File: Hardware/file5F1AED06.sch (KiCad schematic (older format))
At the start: 17 parts, among them U2 RFPA3800

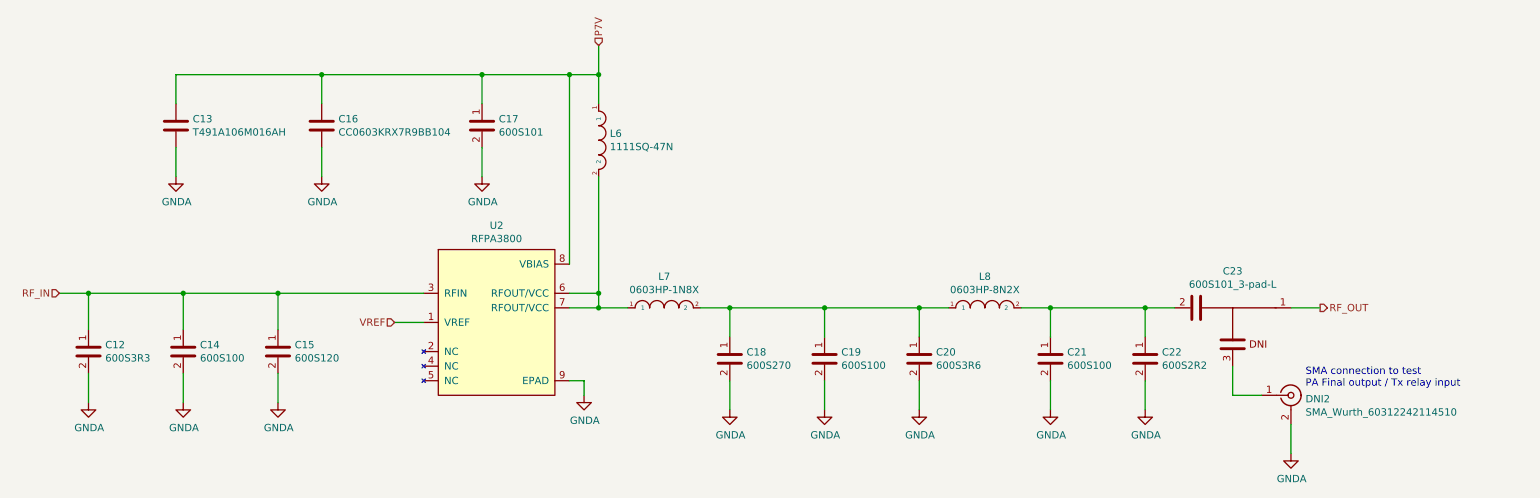
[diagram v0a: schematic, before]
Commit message: Added discrete Chebyshev input filter to schematic based on Qucs simulationd. Artwork not done. It has occurred to me that I need to do some major cleanup of the test points on this PCBA.
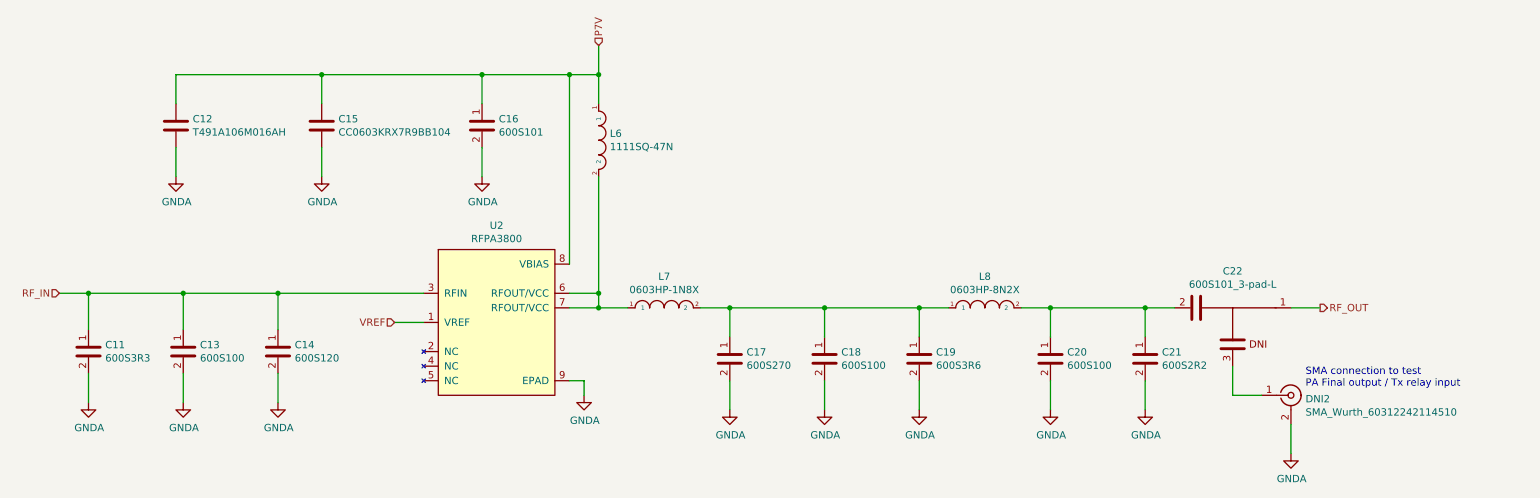
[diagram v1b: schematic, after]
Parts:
- renumbered C12 to C11, C13 to C12, C14 to C13, C15 to C14, C16 to C15, C17 to C16, C18 to C17, C19 to C18, C20 to C19, C21 to C20, C22 to C21, C23 to C22
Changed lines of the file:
@@
 $Descr A4 11693 8268
 encoding utf-8
-Sheet 7 12
+Sheet 7 16
 Title ""
 Date ""
@@
 P 4900 4600
 AR Path="/5F04F5B6/5F1D8FAC" Ref="#PWR?"  Part="1"
-AR Path="/5F04F5B6/5F1AED07/5F1D8FAC" Ref="#PWR026"  Part="1"
-F 0 "#PWR026" H 4900 4350 50  0001 C CNN
+AR Path="/5F04F5B6/5F1AED07/5F1D8FAC" Ref="#PWR023"  Part="1"
+F 0 "#PWR023" H 4900 4350 50  0001 C CNN
 F 1 "GNDA" H 4905 4427 50  0000 C CNN
 F 2 "" H 4900 4600 50  0001 C CNN
@@
 AR Path="/5F19ABE9/5F1D8FD9" Ref="#PWR?"  Part="1"
 AR Path="/5F04F5B6/5F1D8FD9" Ref="#PWR?"  Part="1"
-AR Path="/5F04F5B6/5F1AED07/5F1D8FD9" Ref="#PWR030"  Part="1"
-F 0 "#PWR030" H 8100 4450 50  0001 C CNN
+AR Path="/5F04F5B6/5F1AED07/5F1D8FD9" Ref="#PWR027"  Part="1"
+F 0 "#PWR027" H 8100 4450 50  0001 C CNN
 F 1 "GNDA" H 8105 4527 50  0000 C CNN
 F 2 "" H 8100 4700 50  0001 C CNN
@@
 AR Path="/5F19ABE9/5F1D8FEC" Ref="C?"  Part="1"
 AR Path="/5F04F5B6/5F1D8FEC" Ref="C?"  Part="1"
-AR Path="/5F04F5B6/5F1AED07/5F1D8FEC" Ref="C17"  Part="1"
-F 0 "C17" H 4315 2796 50  0000 L CNN
+AR Path="/5F04F5B6/5F1AED07/5F1D8FEC" Ref="C16"  Part="1"
+F 0 "C16" H 4315 2796 50  0000 L CNN
 F 1 "600S101" H 4315 2705 50  0000 L CNN
 F 2 "Resistor_SMD:R_0603_1608Metric" H 4250 2850 50  0001 C CNN
@@
 AR Path="/5F19ABE9/5F1D8FF2" Ref="#PWR?"  Part="1"
 AR Path="/5F04F5B6/5F1D8FF2" Ref="#PWR?"  Part="1"
-AR Path="/5F04F5B6/5F1AED07/5F1D8FF2" Ref="#PWR024"  Part="1"
-F 0 "#PWR024" H 3100 2850 50  0001 C CNN
+AR Path="/5F04F5B6/5F1AED07/5F1D8FF2" Ref="#PWR021"  Part="1"
+F 0 "#PWR021" H 3100 2850 50  0001 C CNN
 F 1 "GNDA" H 3105 2927 50  0000 C CNN
 F 2 "" H 3100 3100 50  0001 C CNN
@@
 AR Path="/5F19ABE9/5F1D8FF9" Ref="#PWR?"  Part="1"
 AR Path="/5F04F5B6/5F1D8FF9" Ref="#PWR?"  Part="1"
-AR Path="/5F04F5B6/5F1AED07/5F1D8FF9" Ref="#PWR025"  Part="1"
-F 0 "#PWR025" H 4200 2850 50  0001 C CNN
+AR Path="/5F04F5B6/5F1AED07/5F1D8FF9" Ref="#PWR022"  Part="1"
+F 0 "#PWR022" H 4200 2850 50  0001 C CNN
 F 1 "GNDA" H 4205 2927 50  0000 C CNN
 F 2 "" H 4200 3100 50  0001 C CNN
@@
 P 3100 2750
 AR Path="/5F04F5B6/5F1D9008" Ref="C?"  Part="1"
-AR Path="/5F04F5B6/5F1AED07/5F1D9008" Ref="C16"  Part="1"
-F 0 "C16" H 3215 2796 50  0000 L CNN
+AR Path="/5F04F5B6/5F1AED07/5F1D9008" Ref="C15"  Part="1"
+F 0 "C15" H 3215 2796 50  0000 L CNN
 F 1 "CC0603KRX7R9BB104" H 3215 2705 50  0000 L CNN
 F 2 "Capacitor_SMD:C_0603_1608Metric" H 3138 2600 50  0001 C CNN
@@
 P 2150 4300
 AR Path="/5F04F5B6/5F1D9016" Ref="C?"  Part="1"
-AR Path="/5F04F5B6/5F1AED07/5F1D9016" Ref="C14"  Part="1"
-F 0 "C14" H 2265 4346 50  0000 L CNN
+AR Path="/5F04F5B6/5F1AED07/5F1D9016" Ref="C13"  Part="1"
+F 0 "C13" H 2265 4346 50  0000 L CNN
 F 1 "600S100" H 2265 4255 50  0000 L CNN
 F 2 "Capacitor_SMD:C_0603_1608Metric" H 2200 4400 50  0001 C CNN
@@
 P 2800 4300
 AR Path="/5F04F5B6/5F1D901C" Ref="C?"  Part="1"
-AR Path="/5F04F5B6/5F1AED07/5F1D901C" Ref="C15"  Part="1"
-F 0 "C15" H 2915 4346 50  0000 L CNN
+AR Path="/5F04F5B6/5F1AED07/5F1D901C" Ref="C14"  Part="1"
+F 0 "C14" H 2915 4346 50  0000 L CNN
 F 1 "600S120" H 2915 4255 50  0000 L CNN
 F 2 "Capacitor_SMD:C_0603_1608Metric" H 2850 4400 50  0001 C CNN
@@
 P 1500 4300
 AR Path="/5F04F5B6/5F1D9022" Ref="C?"  Part="1"
-AR Path="/5F04F5B6/5F1AED07/5F1D9022" Ref="C12"  Part="1"
-F 0 "C12" H 1615 4346 50  0000 L CNN
+AR Path="/5F04F5B6/5F1AED07/5F1D9022" Ref="C11"  Part="1"
+F 0 "C11" H 1615 4346 50  0000 L CNN
 F 1 "600S3R3" H 1615 4255 50  0000 L CNN
 F 2 "Capacitor_SMD:C_0603_1608Metric" H 1550 4400 50  0001 C CNN
@@
 RF_IN
 $Comp
-L power:GNDA #PWR020
+L power:GNDA #PWR017
 U 1 1 5F1E2B17
 P 1500 4650
-F 0 "#PWR020" H 1500 4400 50  0001 C CNN
+F 0 "#PWR017" H 1500 4400 50  0001 C CNN
 F 1 "GNDA" H 1505 4477 50  0000 C CNN
 F 2 "" H 1500 4650 50  0001 C CNN
@@
 $EndComp
 $Comp
-L power:GNDA #PWR022
+L power:GNDA #PWR019
 U 1 1 5F1E2D76
 P 2150 4650
-F 0 "#PWR022" H 2150 4400 50  0001 C CNN
+F 0 "#PWR019" H 2150 4400 50  0001 C CNN
 F 1 "GNDA" H 2155 4477 50  0000 C CNN
 F 2 "" H 2150 4650 50  0001 C CNN
@@
 $EndComp
 $Comp
-L power:GNDA #PWR023
+L power:GNDA #PWR020
 U 1 1 5F1E3182
 P 2800 4650
-F 0 "#PWR023" H 2800 4400 50  0001 C CNN
+F 0 "#PWR020" H 2800 4400 50  0001 C CNN
 F 1 "GNDA" H 2805 4477 50  0000 C CNN
 F 2 "" H 2800 4650 50  0001 C CNN
@@
 $EndComp
 $Comp
-L ATC:600S270 C18
+L ATC:600S270 C17
 U 1 1 5F1EB80A
 P 5900 4350
-F 0 "C18" H 6015 4396 50  0000 L CNN
+F 0 "C17" H 6015 4396 50  0000 L CNN
 F 1 "600S270" H 6015 4305 50  0000 L CNN
 F 2 "Capacitor_SMD:C_0603_1608Metric" H 5950 4450 50  0001 C CNN
@@
 $EndComp
 $Comp
-L ATC:600S100 C19
+L ATC:600S100 C18
 U 1 1 5F1EBBE5
 P 6550 4350
-F 0 "C19" H 6665 4396 50  0000 L CNN
+F 0 "C18" H 6665 4396 50  0000 L CNN
 F 1 "600S100" H 6665 4305 50  0000 L CNN
 F 2 "Capacitor_SMD:C_0603_1608Metric" H 6600 4450 50  0001 C CNN
@@
 $EndComp
 $Comp
-L ATC:600S3R6 C20
+L ATC:600S3R6 C19
 U 1 1 5F1EBFC8
 P 7200 4350
-F 0 "C20" H 7315 4396 50  0000 L CNN
+F 0 "C19" H 7315 4396 50  0000 L CNN
 F 1 "600S3R6" H 7315 4305 50  0000 L CNN
 F 2 "Capacitor_SMD:C_0603_1608Metric" H 7250 4450 50  0001 C CNN
@@
 $EndComp
 $Comp
-L ATC:600S100 C21
+L ATC:600S100 C20
 U 1 1 5F1EC703
 P 8100 4350
-F 0 "C21" H 8215 4396 50  0000 L CNN
+F 0 "C20" H 8215 4396 50  0000 L CNN
 F 1 "600S100" H 8215 4305 50  0000 L CNN
 F 2 "Capacitor_SMD:C_0603_1608Metric" H 8150 4450 50  0001 C CNN
@@
 $EndComp
 $Comp
-L ATC:600S2R2 C22
+L ATC:600S2R2 C21
 U 1 1 5F1ECAB0
 P 8750 4350
-F 0 "C22" H 8865 4396 50  0000 L CNN
+F 0 "C21" H 8865 4396 50  0000 L CNN
 F 1 "600S2R2" H 8865 4305 50  0000 L CNN
 F 2 "Capacitor_SMD:C_0603_1608Metric" H 8800 4450 50  0001 C CNN
@@
 AR Path="/5F19ABE9/5F1F33B9" Ref="#PWR?"  Part="1"
 AR Path="/5F04F5B6/5F1F33B9" Ref="#PWR?"  Part="1"
-AR Path="/5F04F5B6/5F1AED07/5F1F33B9" Ref="#PWR029"  Part="1"
-F 0 "#PWR029" H 7200 4450 50  0001 C CNN
+AR Path="/5F04F5B6/5F1AED07/5F1F33B9" Ref="#PWR026"  Part="1"
+F 0 "#PWR026" H 7200 4450 50  0001 C CNN
 F 1 "GNDA" H 7205 4527 50  0000 C CNN
 F 2 "" H 7200 4700 50  0001 C CNN
@@
 AR Path="/5F19ABE9/5F1F3A81" Ref="#PWR?"  Part="1"
 AR Path="/5F04F5B6/5F1F3A81" Ref="#PWR?"  Part="1"
-AR Path="/5F04F5B6/5F1AED07/5F1F3A81" Ref="#PWR028"  Part="1"
-F 0 "#PWR028" H 6550 4450 50  0001 C CNN
+AR Path="/5F04F5B6/5F1AED07/5F1F3A81" Ref="#PWR025"  Part="1"
+F 0 "#PWR025" H 6550 4450 50  0001 C CNN
 F 1 "GNDA" H 6555 4527 50  0000 C CNN
 F 2 "" H 6550 4700 50  0001 C CNN
@@
 AR Path="/5F19ABE9/5F1F436D" Ref="#PWR?"  Part="1"
 AR Path="/5F04F5B6/5F1F436D" Ref="#PWR?"  Part="1"
-AR Path="/5F04F5B6/5F1AED07/5F1F436D" Ref="#PWR027"  Part="1"
-F 0 "#PWR027" H 5900 4450 50  0001 C CNN
+AR Path="/5F04F5B6/5F1AED07/5F1F436D" Ref="#PWR024"  Part="1"
+F 0 "#PWR024" H 5900 4450 50  0001 C CNN
 F 1 "GNDA" H 5905 4527 50  0000 C CNN
 F 2 "" H 5900 4700 50  0001 C CNN
@@
 AR Path="/5F19ABE9/5F1F4C55" Ref="#PWR?"  Part="1"
 AR Path="/5F04F5B6/5F1F4C55" Ref="#PWR?"  Part="1"
-AR Path="/5F04F5B6/5F1AED07/5F1F4C55" Ref="#PWR031"  Part="1"
-F 0 "#PWR031" H 8750 4450 50  0001 C CNN
+AR Path="/5F04F5B6/5F1AED07/5F1F4C55" Ref="#PWR028"  Part="1"
+F 0 "#PWR028" H 8750 4450 50  0001 C CNN
 F 1 "GNDA" H 8755 4527 50  0000 C CNN
 F 2 "" H 8750 4700 50  0001 C CNN
@@
 AR Path="/5F04F5B6/5F292502" Ref="#PWR?"  Part="1"
 AR Path="/5F04F5B6/5F1AE89A/5F292502" Ref="#PWR?"  Part="1"
-AR Path="/5F04F5B6/5F1AED07/5F292502" Ref="#PWR032"  Part="1"
-F 0 "#PWR032" H 9750 4750 50  0001 C CNN
+AR Path="/5F04F5B6/5F1AED07/5F292502" Ref="#PWR029"  Part="1"
+F 0 "#PWR029" H 9750 4750 50  0001 C CNN
 F 1 "GNDA" H 9755 4827 50  0000 C CNN
 F 2 "" H 9750 5000 50  0001 C CNN
@@
 SMA connection to test\nPA Final output / Tx relay input
 $Comp
-L Kemet:T491A106M016AH C13
+L Kemet:T491A106M016AH C12
 U 1 1 5F2FD57C
 P 2100 2750
-F 0 "C13" H 2215 2796 50  0000 L CNN
+F 0 "C12" H 2215 2796 50  0000 L CNN
 F 1 "T491A106M016AH" H 2215 2705 50  0000 L CNN
 F 2 "Capacitor_SMD:C_1206_3216Metric" H 2138 2600 50  0001 C CNN
@@
 AR Path="/5F19ABE9/5F2FE672" Ref="#PWR?"  Part="1"
 AR Path="/5F04F5B6/5F2FE672" Ref="#PWR?"  Part="1"
-AR Path="/5F04F5B6/5F1AED07/5F2FE672" Ref="#PWR021"  Part="1"
-F 0 "#PWR021" H 2100 2850 50  0001 C CNN
+AR Path="/5F04F5B6/5F1AED07/5F2FE672" Ref="#PWR018"  Part="1"
+F 0 "#PWR018" H 2100 2850 50  0001 C CNN
 F 1 "GNDA" H 2105 2927 50  0000 C CNN
 F 2 "" H 2100 3100 50  0001 C CNN
@@
 Connection ~ 3100 2400
 $Comp
-L ATC:600S101_3-pad-L C23
+L ATC:600S101_3-pad-L C22
 U 1 1 5F35E2C7
 P 9350 4000
-F 0 "C23" H 9350 3748 50  0000 C CNN
+F 0 "C22" H 9350 3748 50  0000 C CNN
 F 1 "600S101_3-pad-L" H 9350 3839 50  0000 C CNN
 F 2 "Capacitor_SMD:C_0603_1608Metric_3-pad-L" H 10250 3250 50  0001 C CNN

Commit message: Major cleanup to both the schematic and directory structure. Stackup has changed accomodate to 0.65mm trace width. Chebyshev filter lived through the experience in the Qucs simulation; others not checked yet. I do want to re-visit the matching networks of all of the amplifiers as I have developed some good strategies to implement them.
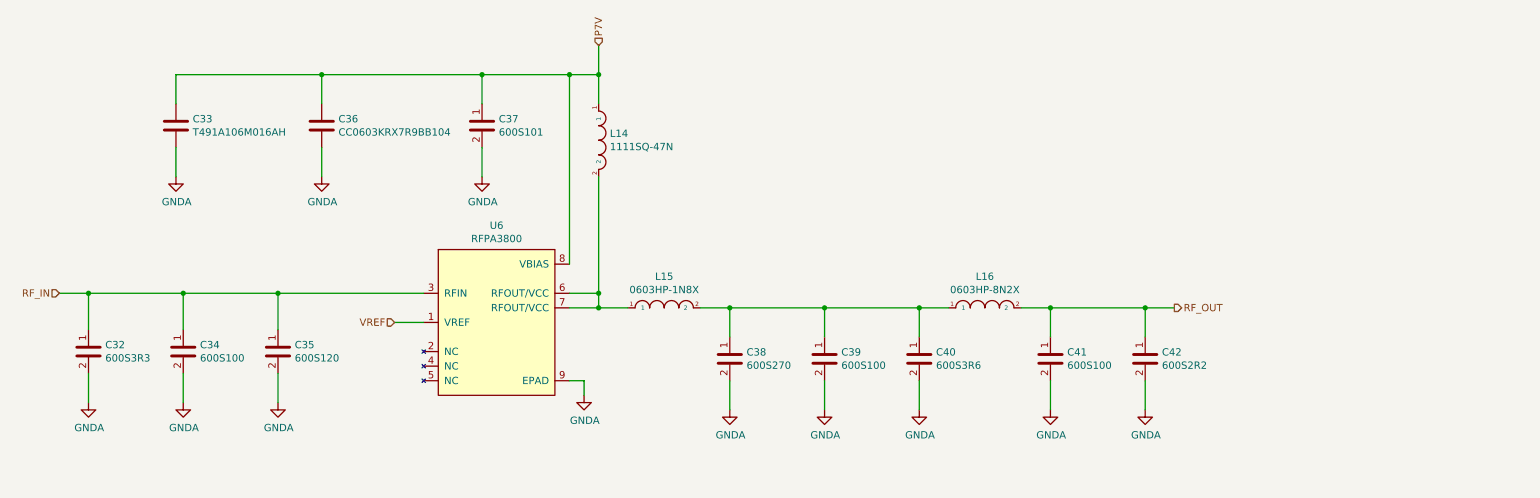
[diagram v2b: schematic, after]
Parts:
- removed C22: 600S101_3-pad-L, Capacitor_SMD:C_0603_1608Metric_3-pad-L, symbol ATC:600S101_3-pad-L
- removed DNI2: SMA_Wurth_60312242114510, RF:SMA_Wurth_60312242114510, symbol RF:SMA_Wurth_60312242114510
- renumbered C11 to C32, C12 to C33, C13 to C34, C14 to C35, C15 to C36, C16 to C37, C17 to C38, C18 to C39, C19 to C40, C20 to C41, C21 to C42, L6 to L14, L7 to L15, L8 to L16, U2 to U6
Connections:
- net RF_OUT: now also C41.1, C42.1, L16.2
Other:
- note removed: "SMA connection to test\nPA Final output / Tx relay input"
